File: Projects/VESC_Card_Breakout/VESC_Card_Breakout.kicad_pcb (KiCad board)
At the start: 2 copper layers, 67.1 x 33.5 mm, 11 parts, among them P1 USB_OTG, P2 CONN_01X02, P3 CONN_01X04, P4 EC90_Flat, P5 CONN_01X02, P6 AMP17614426-2_EDGE, P7 CONN_01X06

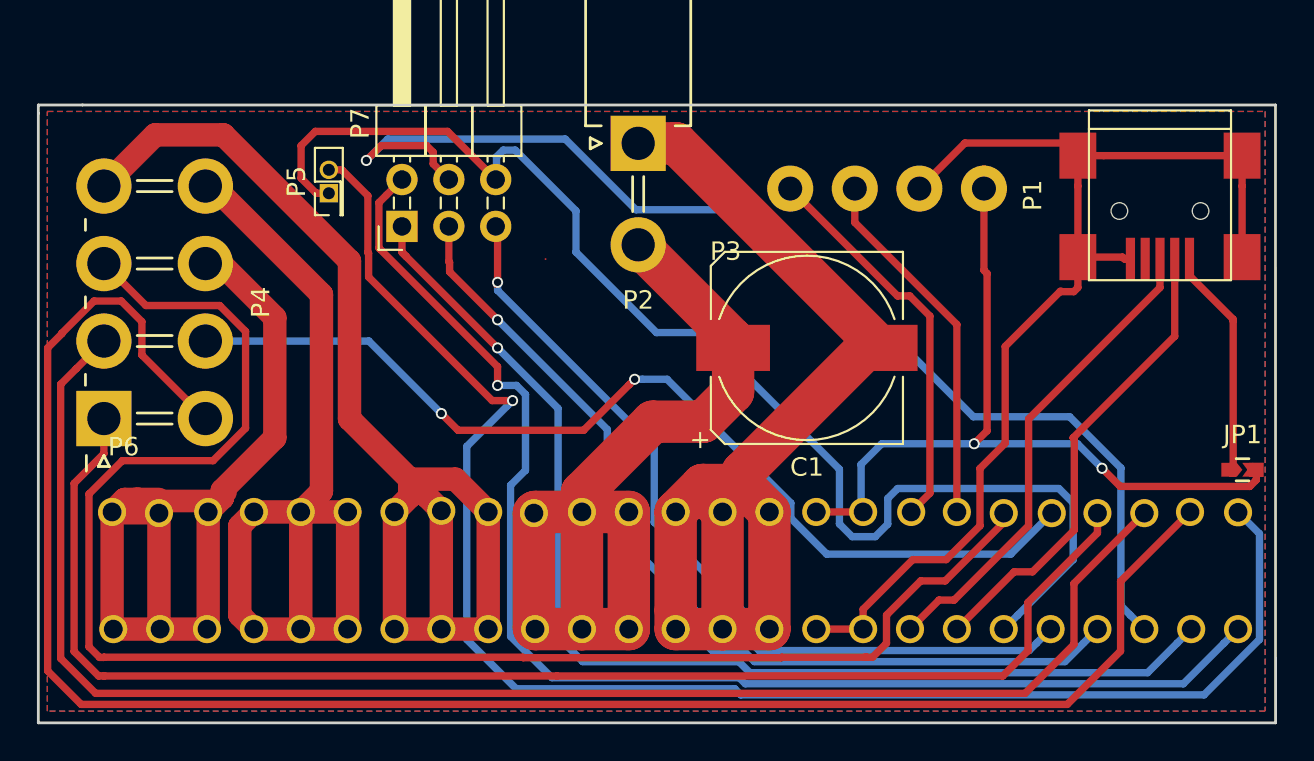
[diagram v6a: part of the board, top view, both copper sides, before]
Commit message: edited VESC Card Breakout, redid footprint
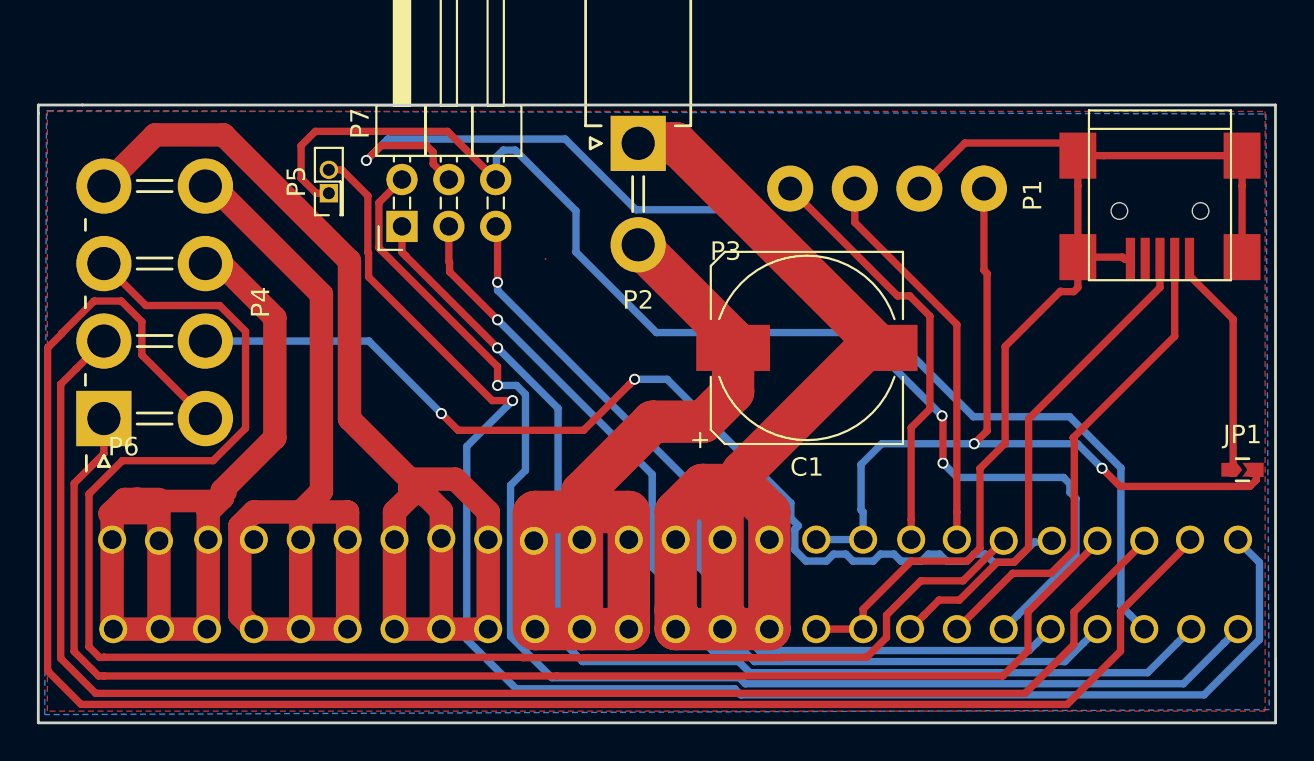
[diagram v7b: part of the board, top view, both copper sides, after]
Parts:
- P6: footprint USST-footprints:TE2007088-1_Backplane -> USST-footprints:TE2007088-1_Backplane2
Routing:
- net /Motor_Controller/Y: track 64.2 -> 68.7 mm
- net /Motor_Controller/VBAT: track 50.9 -> 55.4 mm
- net /Motor_Controller/W: track 52.1 -> 56.5 mm
- net /Motor_Controller/X: track 50.8 -> 54.9 mm
- net /Motor_Controller/GND_AUX: track 69.9 -> 67.3 mm, vias 0 -> 2
- net Net-(P4-Pad6): track 54.3 -> 56.5 mm
- net /5v0: track 44.3 -> 46.3 mm
- net /Motor_Controller/H3: track 100.0 -> 98.4 mm
- net /Motor_Controller/H1: track 75.2 -> 73.6 mm
- net Net-(P5-Pad2): track 84.5 -> 82.9 mm
- net /Motor_Controller/H2: track 83.7 -> 82.1 mm
- net /Motor_Controller/CANL/RX: track 19.8 -> 21.3 mm
- net /Motor_Controller/CANH/TX: track 21.5 -> 23.0 mm
- net Net-(P4-Pad3): track 87.1 -> 86.0 mm
- net /GNDD: track 66.2 -> 66.9 mm
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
